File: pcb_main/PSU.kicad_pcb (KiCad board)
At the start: 2 copper layers, 30 parts, among them IC101 OPA277, IC102 OPA277, Q101 BD249C, Q102 BD139, Q103 BD249C, Q104 BC557, Q105 BD139, Q106 BD249C, Q107 BD139, U101 ATmega8A-A, U102 MC78L05, U103 MC79L05

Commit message: +-5V reg
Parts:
- moved IC101 128.2 mm to (115.0, 84.0)
- moved IC102 127.2 mm to (104.5, 84.0)
- moved D102 96.9 mm to (105.0, 76.0), turned to 90 degrees
- moved Q102 92.8 mm to (65.5, 120.5)
- moved Q105 92.8 mm to (90.0, 120.5)
- moved Q107 92.8 mm to (114.5, 120.5)
- moved R104 92.8 mm to (107.1, 130.0)
- moved Q101 92.8 mm to (69.5, 120.9)
- moved Q103 92.8 mm to (94.0, 120.9)
- moved Q106 92.8 mm to (118.5, 120.9)
- moved R101 92.8 mm to (82.6, 130.0)
- moved R105 92.8 mm to (131.6, 130.0)
- moved D101 83.3 mm to (115.5, 76.5), turned to 90 degrees
- moved R103 74.5 mm to (141.0, 89.0), turned to 90 degrees
- moved U101 20.6 mm to (240.5, 56.5)
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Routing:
- net VCC: track 0.00 -> 96.1 mm
- net /pwr_e: track 0.00 -> 82.7 mm
- net /pwr_b: track 0.00 -> 59.1 mm
- net /pwr_e3: track 0.00 -> 10.0 mm
- net /pwr_e2: track 0.00 -> 10.0 mm
- net /pwr_e1: track 0.00 -> 10.0 mm
- net Net-(Q101-Pad1): track 0.00 -> 4.70 mm
- net Net-(Q106-Pad1): track 0.00 -> 4.15 mm
- net Net-(Q103-Pad1): track 0.00 -> 4.15 mm
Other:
- board outline added: 100 x 100 mm

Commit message: hierarchical design
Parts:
- removed C101: 10u, Resistor_SMD:R_0603_1608Metric
- removed C102, C104: 22p, Resistor_SMD:R_0603_1608Metric
- removed C103: 10n, Capacitor_SMD:C_0603_1608Metric
- removed D101, D102, D103, D104: 1N4148WS, Diode_SMD:D_SOD-323
- removed IC101, IC102: OPA277, OPA277:SO08
- removed Q104: BC557, Package_TO_SOT_SMD:SOT-23
- removed R102, R106, R107, R108, R109: 100R, Resistor_SMD:R_0603_1608Metric
- removed R103: 15m, Resistor_SMD:R_2512_6332Metric
- removed RV101: 4k7, Potentiometer_THT:Potentiometer_Vishay_T73YP_Vertical
- removed U101: ATmega8A-A, Package_QFP:TQFP-32_7x7mm_P0.8mm
- removed U102: MC78L05, Package_TO_SOT_SMD:SOT-89-3
- removed U103: MC79L05, Package_TO_SOT_SMD:SOT-89-3
- added C201: 1000u, Capacitor_THT:CP_Radial_D8.0mm_P3.50mm, F.Cu at (77.5, 42.8)
- added C202: 100n, Capacitor_SMD:C_0603_1608Metric, F.Cu at (86.9, 48.2)
- added C203: 100n, Capacitor_SMD:C_0603_1608Metric, F.Cu at (87.6, 50.3)
- added C204: 1000u, Capacitor_THT:CP_Radial_D8.0mm_P3.50mm, F.Cu at (77.5, 55.0)
- added C205: 1000u, Capacitor_THT:CP_Radial_D8.0mm_P3.50mm, F.Cu at (78.0, 65.5)
- added C301: 10u, Resistor_SMD:R_0603_1608Metric, F.Cu at (105.4, 81.5)
- added C302: 22p, Resistor_SMD:R_0603_1608Metric, F.Cu at (86.7, 84.7)
- added C303: 10n, Capacitor_SMD:C_0603_1608Metric, F.Cu at (96.3, 87.1)
- added C304: 22p, Resistor_SMD:R_0603_1608Metric, F.Cu at (139.2, 62.5)
- added C401: 470n, Capacitor_SMD:C_0603_1608Metric, F.Cu at (112.1, 65.2)
- added C402: 100n, Capacitor_SMD:C_0603_1608Metric, F.Cu at (132.7, 71.4)
- added C403: 100n, Capacitor_SMD:C_0603_1608Metric, F.Cu at (138.8, 77.7)
- added D201: 1N5819, Diode_THT:D_DO-41_SOD81_P10.16mm_Horizontal, F.Cu at (71.1, 46.7)
- added D202: 1N5819, Diode_THT:D_DO-41_SOD81_P10.16mm_Horizontal, F.Cu at (71.1, 43.4)
- added D203: 1N5819, Diode_THT:D_DO-41_SOD81_P10.16mm_Horizontal, F.Cu at (61.0, 50.0)
- added D204: 1N5819, Diode_THT:D_DO-41_SOD81_P10.16mm_Horizontal, F.Cu at (61.0, 53.4)
- added D205: 1N5819, Diode_THT:D_DO-41_SOD81_P10.16mm_Horizontal, F.Cu at (71.4, 61.1)
- added D206: 1N5819, Diode_THT:D_DO-41_SOD81_P10.16mm_Horizontal, F.Cu at (71.4, 64.4)
- added D207: 1N5819, Diode_THT:D_DO-41_SOD81_P10.16mm_Horizontal, F.Cu at (61.2, 71.1)
- added D208: 1N5819, Diode_THT:D_DO-41_SOD81_P10.16mm_Horizontal, F.Cu at (61.2, 67.8)
- added D301: 1N4148WS, Diode_SMD:D_SOD-323, F.Cu at (124.0, 79.2)
- added D302: 1N4148WS, Diode_SMD:D_SOD-323, F.Cu at (143.3, 55.4)
- added D303: 1N4148WS, Diode_SMD:D_SOD-323, F.Cu at (142.1, 72.1)
- added D304: 1N4148WS, Diode_SMD:D_SOD-323, F.Cu at (142.1, 70.1)
- added IC301: OPA277, OPA277:SO08, F.Cu at (123.2, 86.4)
- added IC302: OPA277, OPA277:SO08, F.Cu at (142.5, 62.5)
- added J101: JST_XH_B2B-XH, Connector_JST:JST_XH_B2B-XH-A_1x02_P2.50mm_Vertical, F.Cu at (145.5, 89.3)
- added J102: JST_XH_B2B-XH, Connector_JST:JST_XH_B2B-XH-A_1x02_P2.50mm_Vertical, F.Cu at (54.8, 130.0)
- added J103: JST_XH_B3B-XH, Connector_JST:JST_XH_B3B-XH-A_1x03_P2.50mm_Vertical, F.Cu at (54.1, 49.5)
- added J104: JST_XH_B2B-XH, Connector_JST:JST_XH_B2B-XH-A_1x02_P2.50mm_Vertical, F.Cu at (54.4, 67.1)
- added Q304: BC557, Package_TO_SOT_SMD:SOT-23, F.Cu at (104.4, 84.8)
- added Q401: 2N7002, Package_TO_SOT_SMD:SOT-23, F.Cu at (124.0, 48.3)
- added Q402: 2N7002, Package_TO_SOT_SMD:SOT-23, F.Cu at (119.3, 48.3)
- added R302: 100R, Resistor_SMD:R_0603_1608Metric, F.Cu at (103.1, 81.5)
- added R303: 15m, Resistor_SMD:R_2512_6332Metric, F.Cu at (143.0, 98.5)
- added R306: 100R, Resistor_SMD:R_0603_1608Metric, F.Cu at (137.7, 100.1)
- added R307: 100R, Resistor_SMD:R_0603_1608Metric, F.Cu at (96.3, 83.8)
- added R308: 100R, Resistor_SMD:R_0603_1608Metric, F.Cu at (96.3, 85.5)
- added R309: 100R, Resistor_SMD:R_0603_1608Metric, F.Cu at (141.0, 68.2)
- added R401: 4k7, Resistor_SMD:R_0603_1608Metric, F.Cu at (117.7, 44.6)
- added R402: 4k7, Resistor_SMD:R_0603_1608Metric, F.Cu at (127.0, 46.1)
- added R403: 4k7, Resistor_SMD:R_0603_1608Metric, F.Cu at (124.0, 51.1)
- added R404: 4k7, Resistor_SMD:R_0603_1608Metric, F.Cu at (119.3, 51.1)
- added R405: 4k7, Resistor_SMD:R_0603_1608Metric, F.Cu at (134.6, 80.8)
- added R406: 4k7, Resistor_SMD:R_0603_1608Metric, F.Cu at (134.6, 82.4)
- added RV301: 4k7, Potentiometer_THT:Potentiometer_Vishay_T73YP_Vertical, F.Cu at (111.8, 85.8)
- added U201: MC78L05, Package_TO_SOT_SMD:SOT-89-3, F.Cu at (87.6, 44.7)
- added U202: MC79L05, Package_TO_SOT_SMD:SOT-89-3, F.Cu at (87.6, 53.9)
- added U401: REF3240, Package_TO_SOT_SMD:SOT-23-6, F.Cu at (116.0, 64.6)
- added U402: MCP4725, Package_TO_SOT_SMD:SOT-23-6, F.Cu at (132.7, 75.7)
- added U403: ATmega328P-A, Package_QFP:TQFP-32_7x7mm_P0.8mm, F.Cu at (108.3, 52.1)
- added U404: MCP4725, Package_TO_SOT_SMD:SOT-23-6, F.Cu at (138.8, 81.8)
- renumbered Q101 to Q301, Q102 to Q302, Q103 to Q303, Q105 to Q305, Q106 to Q306, Q107 to Q307, R101 to R301, R104 to R304, R105 to R305
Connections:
- net /pwr_b renamed /main linear regulator/pwr_b
- net /pwr_e renamed /main linear regulator/pwr_e
- net /pwr_e1 renamed /main linear regulator/pwr_e1
- net /pwr_e2 renamed /main linear regulator/pwr_e2
- net /pwr_e3 renamed /main linear regulator/pwr_e3
- net VCC renamed /main linear regulator/+Vin
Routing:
- net /+7VAC: track 0.00 -> 22.4 mm
- net /-7VAC: track 0.00 -> 10.7 mm
- net Net-(C304-Pad2): track 0.00 -> 7.65 mm
- net Net-(C303-Pad2): track 0.00 -> 7.07 mm
- net Net-(C304-Pad1): track 0.00 -> 5.78 mm
- net +4V: track 0.00 -> 3.81 mm
- net /power/-9V_unreg: track 0.00 -> 3.31 mm
- net /power/+9V_unreg: track 0.00 -> 3.31 mm

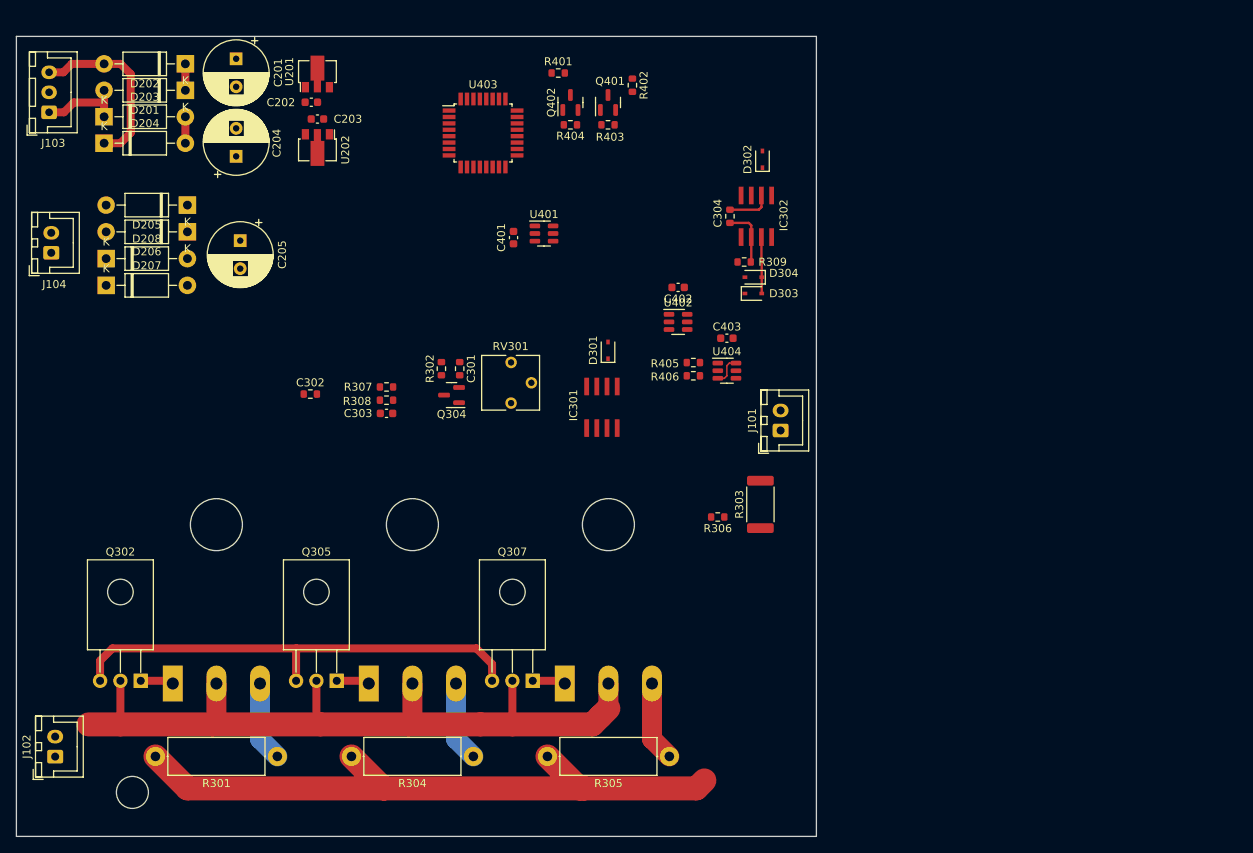
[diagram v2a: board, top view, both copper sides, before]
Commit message: power tracks routed
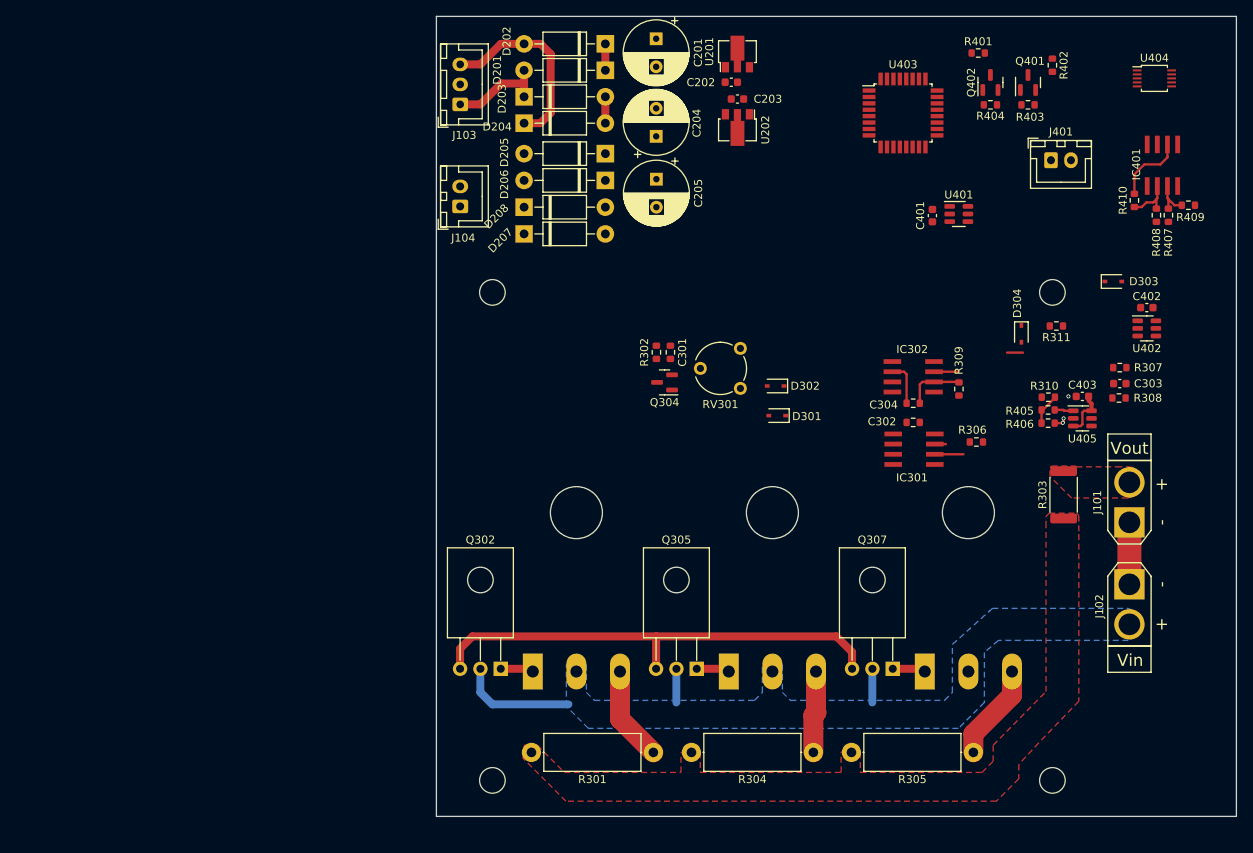
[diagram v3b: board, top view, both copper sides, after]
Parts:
- added IC401: OPA277, OPA277:SO08, F.Cu at (193.2, 56.1)
- added J401: JST_XH_B2B-XH, Connector_JST:JST_XH_B2B-XH-A_1x02_P2.50mm_Vertical, F.Cu at (179.3, 55.5)
- added R310: 10k, Resistor_SMD:R_0603_1608Metric, F.Cu at (179.0, 85.1)
- added R311: 4k7, Resistor_SMD:R_0603_1608Metric, F.Cu at (180.0, 76.2)
- added R407: 100k, Resistor_SMD:R_0603_1608Metric, F.Cu at (194.0, 62.4)
- added R408: 100k, Resistor_SMD:R_0603_1608Metric, F.Cu at (192.5, 62.4)
- added R409: 10k, Resistor_SMD:R_0603_1608Metric, F.Cu at (196.5, 61.1)
- added R410: 10k, Resistor_SMD:R_0603_1608Metric, F.Cu at (189.8, 60.5)
- added U404: ADS1115IDGS, Package_SO:TSSOP-10_3x3mm_P0.5mm, F.Cu at (192.2, 45.2)
- C303: value 10n -> 1n
- J101, J102: value JST_XH_B2B-XH -> XT30; footprint Connector_JST:JST_XH_B2B-XH-A_1x02_P2.50mm_Vertical -> Connector_AMASS:AMASS_XT30U-M_1x02_P5.0mm_Vertical
- R302: value 100R -> 220R
- R306: value 100R -> 22k
- R307: value 100R -> 10k?
- R308: value 100R -> 100k?
- R309: value 100R -> 10k
- RV301: footprint Potentiometer_THT:Potentiometer_Vishay_T73YP_Vertical -> Potentiometer_THT:Potentiometer_Piher_PT-6-V_Vertical
- moved J102 136.0 mm to (189.1, 108.5), turned to -90 degrees
- moved C303 91.7 mm to (187.9, 83.4), turned to 180 degrees
- moved R307 91.7 mm to (187.9, 81.4), turned to 180 degrees
- moved R308 91.6 mm to (187.8, 85.2), turned to 0 degrees
- moved C302 75.4 mm to (162.1, 88.2)
- moved C402 58.6 mm to (191.3, 73.9), turned to 0 degrees
- moved U402 58.6 mm to (191.3, 76.5)
- moved D205 52.6 mm to (123.6, 54.7)
- moved D206 52.6 mm to (123.6, 58.0)
- moved D207 52.6 mm to (113.5, 64.7)
- moved D208 52.6 mm to (113.5, 61.3)
- moved C205 52.6 mm to (130.0, 57.8)
- moved R401 52.6 mm to (170.2, 42.1)
- moved C201 52.6 mm to (130.0, 40.3)
- moved C202 52.6 mm to (139.4, 45.7)
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- renumbered U404 to U405
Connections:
- net /+7VAC renamed /power/+7VAC
- net /-7VAC renamed /power/-7VAC
- net /main linear regulator/I_amp_inv renamed /main linear regulator/-in_CC_amp
- net Net-(C301-Pad2) renamed /main linear regulator/ccs_b
- net Net-(C304-Pad2) renamed /main linear regulator/-in_CV_amp
- net Net-(Q301-Pad1) renamed /main linear regulator/pwr_eb1
- net Net-(Q303-Pad1) renamed /main linear regulator/pwr_eb2
- net Net-(Q304-Pad3) renamed /main linear regulator/ccs_e
- net Net-(Q306-Pad1) renamed /main linear regulator/pwr_eb3
- net Net-(R405-Pad1) renamed /MCU/I_DAC_out
- C302 pad 1: Net-(C302-Pad1) -> /main linear regulator/out_CV_amp
- C303 pad 2: Net-(C303-Pad2) -> /main linear regulator/Vout_div
- C304 pad 1: Net-(C304-Pad1) -> /main linear regulator/out_CV_amp
- D205 pad 2: /power/12VAC2 -> /power/12VAC1
- D206 pad 2: /power/12VAC1 -> /power/12VAC2
- D207 pad 1: /power/12VAC2 -> /power/12VAC1
- D208 pad 1: /power/12VAC1 -> /power/12VAC2
- D301 pad 1: Net-(C302-Pad1) -> /main linear regulator/out_CV_amp
- D302 pad 1: Net-(C304-Pad1) -> /main linear regulator/out_CV_amp
- D303 pad 2: Net-(C303-Pad2) -> /main linear regulator/+in_CV_amp
- D304 pad 1: Net-(C303-Pad2) -> /main linear regulator/+in_CV_amp
- IC301 pad 3: /MCU/I_set -> /main linear regulator/+in_CC_amp
- IC301 pad 6: Net-(C302-Pad1) -> /main linear regulator/out_CV_amp
- IC302 pad 3: Net-(C303-Pad2) -> /main linear regulator/+in_CV_amp
- IC302 pad 6: Net-(C304-Pad1) -> /main linear regulator/out_CV_amp
- J101 pad 1: GND -> /main linear regulator/-Vin
- J101 pad 2: /main linear regulator/-Vin -> GND
- R307 pad 2: Net-(C303-Pad2) -> /main linear regulator/Vout_div
- R308 pad 1: Net-(C303-Pad2) -> /main linear regulator/Vout_div
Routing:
- net /main linear regulator/pwr_e: track 82.7 -> 0.00 mm
- net /main linear regulator/+Vin: track 96.1 -> 23.0 mm
- net /MCU/Vout_meas: track 0.00 -> 9.05 mm
- net /main linear regulator/-Vin: track 0.00 -> 7.75 mm
- net Net-(C303-Pad2): track 7.07 -> 0.00 mm
- net /MCU/-in_s_amp: track 0.00 -> 6.02 mm
- net Net-(C304-Pad1): track 5.78 -> 0.00 mm
- net /main linear regulator/out_CV_amp: track 0.00 -> 5.78 mm
- net /MCU/+in_s_amp: track 0.00 -> 4.86 mm
- net /MCU/I_set: track 0.00 -> 4.03 mm
- net /main linear regulator/-in_CC_amp: track 0.00 -> 3.58 mm
- net /main linear regulator/+in_CV_amp: track 0.00 -> 3.04 mm
- net /MCU/I_DAC_out: track 0.00 -> 2.37 mm
- net /main linear regulator/pwr_e3: track 10.0 -> 12.1 mm
- net +4V: track 3.81 -> 5.90 mm
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- added copper zone on B.Cu, net /main linear regulator/+Vin
- added copper zone on F.Cu, net /main linear regulator/pwr_e
- added copper zone on F.Cu, net GND
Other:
- outline, holes or cut-outs redrawn
- board text added: "Vin"
- board text added: "Vout"

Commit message: most layout done
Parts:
- added C404: 100n, Capacitor_SMD:C_0603_1608Metric, B.Cu at (178.8, 79.5)
- added C405: 100n, Capacitor_SMD:C_0603_1608Metric, B.Cu at (181.3, 83.0)
- added C406: 20p, Capacitor_SMD:C_0603_1608Metric, F.Cu at (156.6, 52.4)
- added C407: 20p, Capacitor_SMD:C_0603_1608Metric, F.Cu at (162.6, 52.4)
- added C408: 100n, Capacitor_SMD:C_0603_1608Metric, B.Cu at (172.1, 73.6)
- added J402: JST_XH_B4B-XH, Connector_JST:JST_XH_B4B-XH-A_1x04_P2.50mm_Vertical, F.Cu at (137.9, 66.3)
- added J403: JST_XH_B4B-XH, Connector_JST:JST_XH_B4B-XH-A_1x04_P2.50mm_Vertical, F.Cu at (146.3, 66.3)
- added J404: Goldpin_2x3, Connector_PinHeader_2.54mm:PinHeader_2x03_P2.54mm_Vertical, F.Cu at (168.1, 57.3)
- added Y401: 16MHz, Crystal:Crystal_SMD_SeikoEpson_TSX3225-4Pin_3.2x2.5mm, F.Cu at (159.6, 52.4)
- C302, C304: footprint Resistor_SMD:R_0603_1608Metric -> Capacitor_SMD:C_0603_1608Metric
- C401, C402, C403, D303, D304: moved to B.Cu
- moved J103 50.3 mm to (111.7, 98.4), turned to 180 degrees
- moved D202 43.6 mm to (105.6, 80.6), turned to -90 degrees
- moved D203 43.3 mm to (112.2, 90.8), turned to 90 degrees
- moved C203 42.3 mm to (133.7, 89.6)
- moved U202 42.3 mm to (133.7, 93.2)
- moved C202 41.5 mm to (133.0, 86.7)
- moved U201 41.5 mm to (133.8, 83.2)
- moved D204 40.0 mm to (115.5, 90.8), turned to 90 degrees
- moved D201 39.2 mm to (108.9, 80.6), turned to -90 degrees
- moved C201 36.5 mm to (122.0, 75.9)
- moved U404 34.8 mm to (172.0, 73.5)
- moved C204 33.7 mm to (122.0, 85.2), turned to -90 degrees
- moved U402 31.7 mm to (159.8, 73.2), turned to 90 degrees
- moved C402 31.1 mm to (160.2, 74.7)
- moved J401 29.5 mm to (188.6, 83.5), turned to 90 degrees
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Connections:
- R301 pad 2: /main linear regulator/pwr_e -> I_meas
- R303 pad 1: /main linear regulator/pwr_e -> I_meas
- R304 pad 2: /main linear regulator/pwr_e -> I_meas
- R305 pad 2: /main linear regulator/pwr_e -> I_meas
- R306 pad 1: /main linear regulator/pwr_e -> I_meas
- U403 pad 15: unconnected-(U403-Pad15) -> /MCU/MOSI
- U403 pad 16: unconnected-(U403-Pad16) -> /MCU/MISO
- U403 pad 17: unconnected-(U403-Pad17) -> /MCU/SCK
- U403 pad 29: unconnected-(U403-Pad29) -> /MCU/RST
- U403 pad 7: unconnected-(U403-Pad7) -> /MCU/XTAL1
- U403 pad 8: unconnected-(U403-Pad8) -> /MCU/XTAL2
- U404 pad 1: unconnected-(U404-Pad1) -> GND
- U404 pad 10: unconnected-(U404-Pad10) -> /MCU/SCL
- U404 pad 2: unconnected-(U404-Pad2) -> /MCU/ADC_RDY
- U404 pad 4: unconnected-(U404-Pad4) -> /MCU/Vout_meas
- U404 pad 5: unconnected-(U404-Pad5) -> GND
- U404 pad 9: unconnected-(U404-Pad9) -> /MCU/SDA
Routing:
- net GND: track 1.62 -> 132.8 mm, vias 3 -> 10
- net +4V: track 5.90 -> 59.3 mm, vias 0 -> 6
- net /main linear regulator/-Vin: track 7.75 -> 48.4 mm
- net I_meas: track 0.00 -> 37.4 mm, vias 0 -> 2
- net /main linear regulator/pwr_b: track 59.1 -> 93.6 mm
- net /MCU/SDA: track 0.00 -> 29.7 mm, vias 0 -> 2
- net /power/+7VAC: track 24.1 -> 0.00 mm
- net /MCU/SCL: track 0.00 -> 23.9 mm, vias 0 -> 2
- net /MCU/SDA_4V: track 0.00 -> 20.7 mm, vias 0 -> 2
- net +5V: track 0.00 -> 19.0 mm, vias 0 -> 2
- net /MCU/SCL_4V: track 0.00 -> 18.8 mm
- net /main linear regulator/-in_CC_amp: track 3.58 -> 20.7 mm
- net /main linear regulator/out_CV_amp: track 5.78 -> 22.3 mm
- net /MCU/I_DAC_out: track 2.37 -> 18.5 mm, vias 0 -> 2
- net /MCU/-Vout_sense: track 0.00 -> 15.2 mm
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- added copper zone on F.Cu, net I_meas
- removed copper zone on F.Cu, net /main linear regulator/pwr_e
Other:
- board size 100 x 100 mm -> 92 x 100 mm
- board text added: "+Vout_S"
- board text added: "-Vout_S"
- board text added: "22.02.2024"
- board text added: "ADJ base current"
- board text added: "Author:"
- board text added: "Date:"
- board text added: "Dominik Pluta"
- board text added: "Linear power supply 2"
- board text added: "V1.0"
